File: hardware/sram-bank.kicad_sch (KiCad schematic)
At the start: 12 parts, among them U1 74LVC138A, U13 74LVC138A

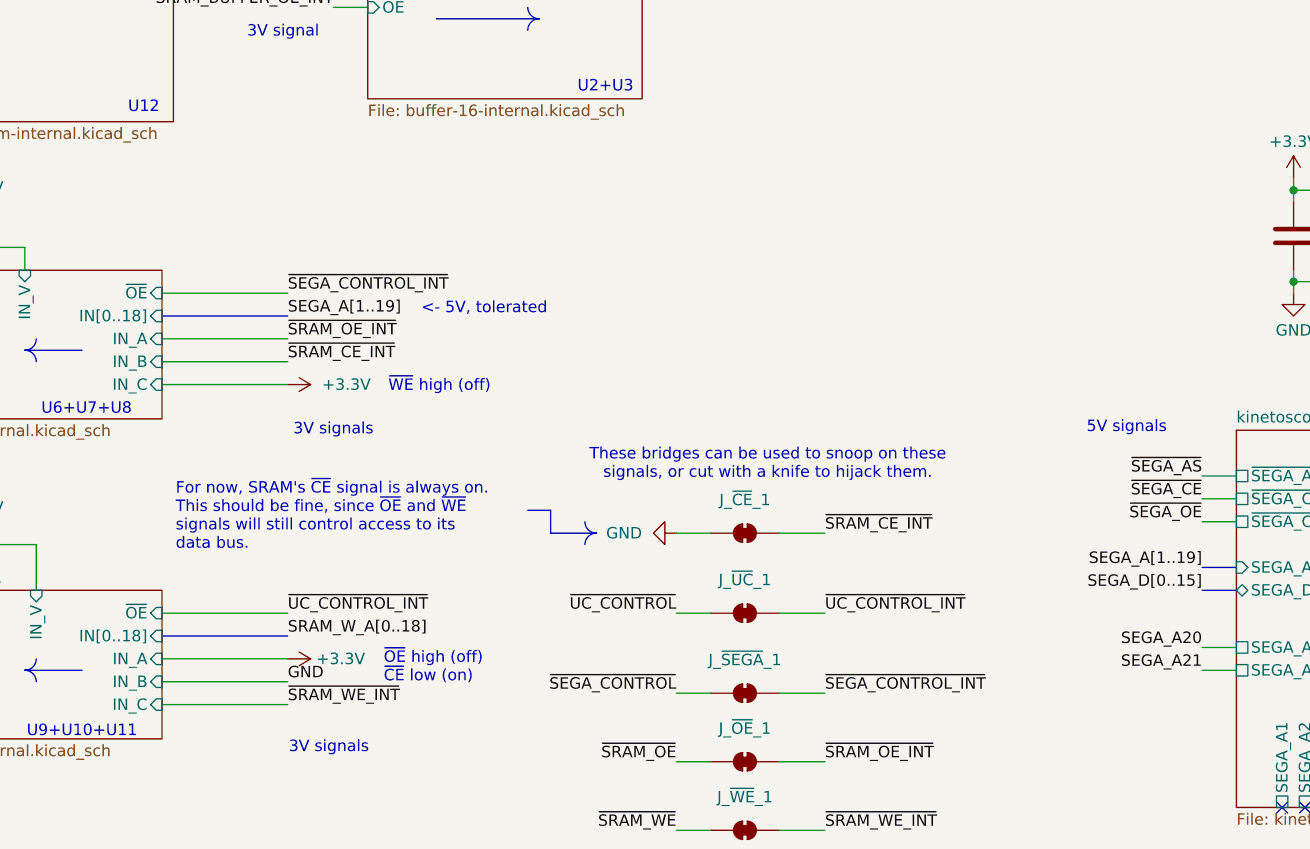
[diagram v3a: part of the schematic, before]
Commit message: Fix SRAM CE signaling
It turns out that a PSRAM's ~{CE} signal may not stay on at all times.
There is a maximum pulse width of 15us for this chipset, so that the
DRAM internal to the PSRAM can go through a refresh cycle.

Tying ~{CE} to ~{WE} (for writes) or ~{SEGA_CE} (for reads) seems to
meet all the timing requirements.  This has yet to be verified,
though, for a lack of test pads for all ~{CE} signals on the previous
board revision.

(PCB routing in progress, will commit later.)
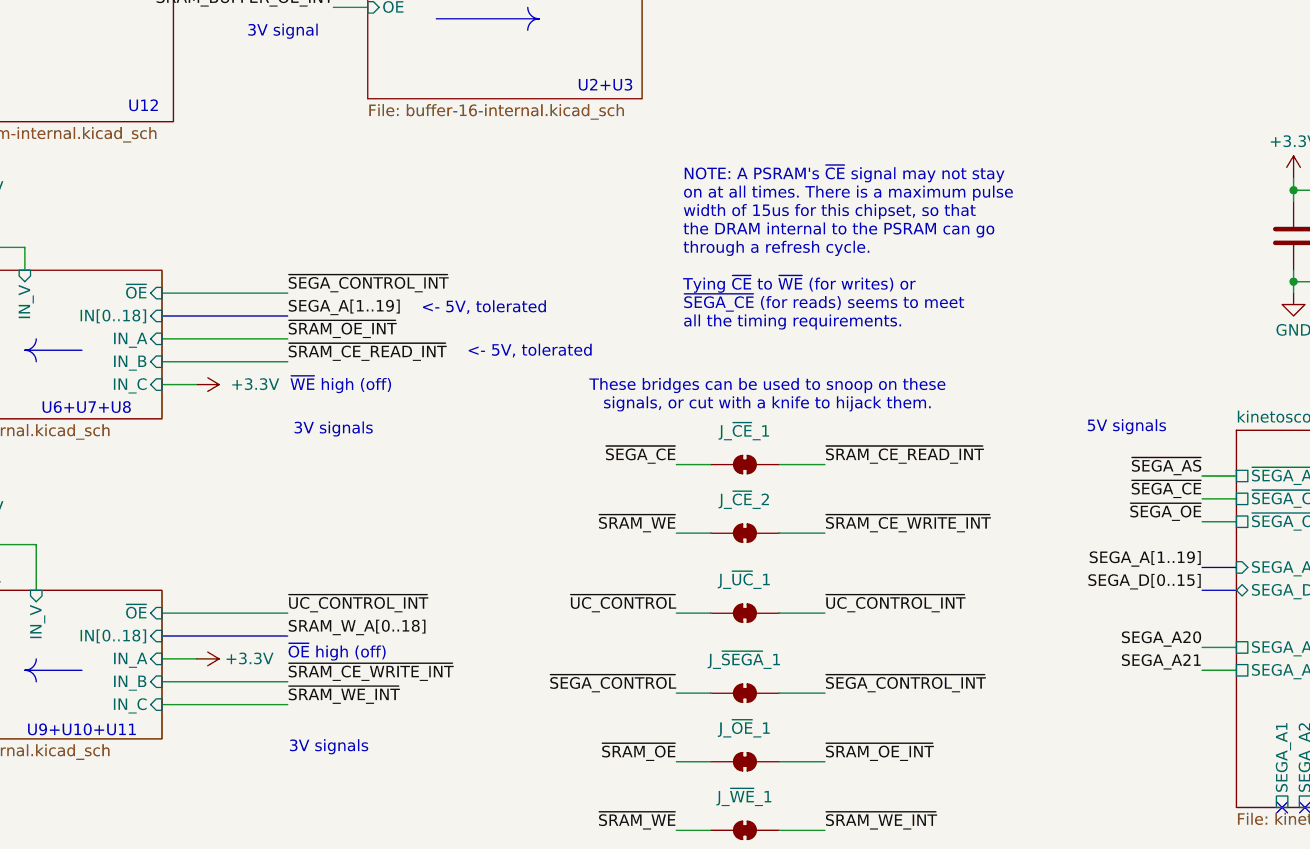
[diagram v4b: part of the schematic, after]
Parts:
- added J_~{CE}_1: ~, Jumper:SolderJumper-2_P1.3mm_Bridged_RoundedPad1.0x1.5mm, symbol Jumper:SolderJumper_2_Bridged
- renumbered J_~{CE}_1 to J_~{CE}_2
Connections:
- net GND: no longer J_~{CE}_2.1 (A)
- net ~{SEGA_CE}: now also J_~{CE}_1.1 (A)
- net ~{SRAM_WE}: now also J_~{CE}_2.1 (A)
- net ~{SRAM_CE_INT} renamed ~{SRAM_CE_WRITE_INT}
- new net ~{SRAM_CE_READ_INT}: J_~{CE}_1.2 (B)
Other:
- note added: "NOTE: A PSRAM's ~{CE} signal may not stay on at all times. There is a maximum pulse width of 15us for this chipset, so that the DRAM internal to the PSRAM can go through a refresh cycle. Tying ~{CE} to ~{WE} (for writes) or ~{SEGA_CE} (for reads) seems to meet all the timing requirements."
- note added: "~{OE} high (off)"
- note removed: "For now, SRAM's ~{CE} signal is always on. This should be fine, since ~{OE} and ~{WE} signals will still control access to its data bus."
- note removed: "~{OE} high (off) ~{CE} low (on)"
